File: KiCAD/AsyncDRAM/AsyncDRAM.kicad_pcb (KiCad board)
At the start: 2 copper layers, 54.6 x 33.7 mm, 14 parts, among them J1 UART, J2 SPI, J3 UPDI, J4 POWER

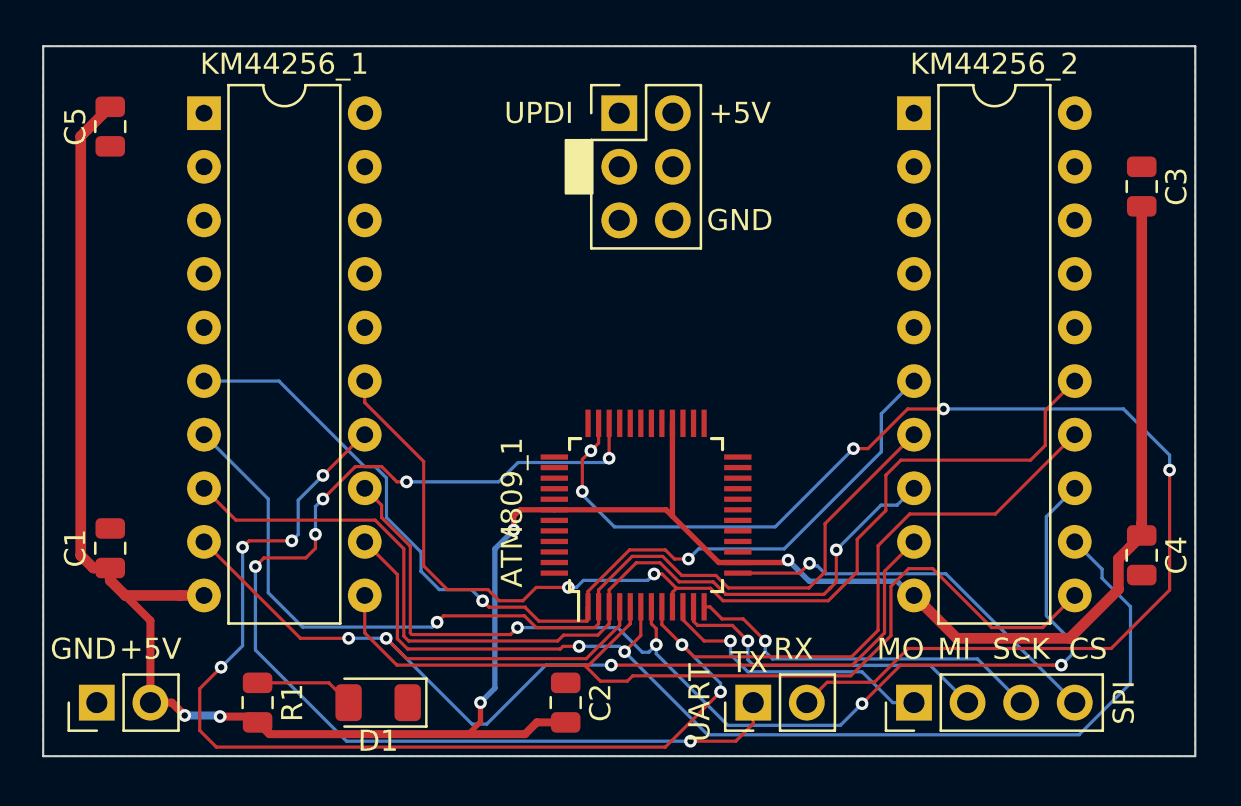
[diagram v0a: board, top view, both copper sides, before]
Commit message: PCB Routing Update
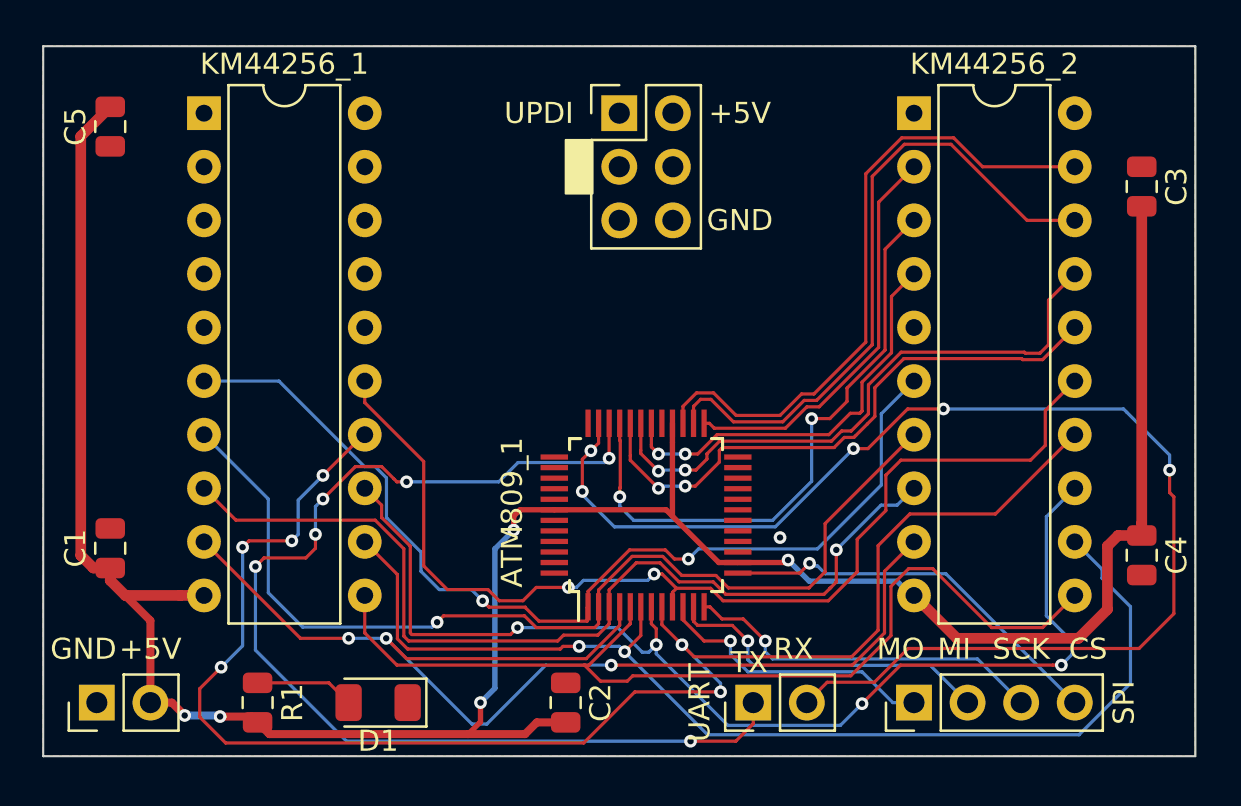
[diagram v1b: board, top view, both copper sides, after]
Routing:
- net D6: track 0.00 -> 31.1 mm
- net D7: track 0.00 -> 30.8 mm
- net ~W: track 0.00 -> 29.3 mm, vias 0 -> 2
- net ~CAS: track 0.00 -> 28.4 mm, vias 0 -> 2
- net ~OE: track 0.00 -> 27.8 mm, vias 0 -> 2
- net ~RAS: track 0.00 -> 19.6 mm, vias 0 -> 2
- net D5: track 0.00 -> 19.2 mm
- net RxD: track 61.2 -> 62.1 mm
- net A0: track 46.9 -> 47.9 mm
- net +5V: track 121.6 -> 122.5 mm
- net A7: track 75.3 -> 74.8 mm
- net GND: vias 0 -> 1

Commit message: Update PCB Routing
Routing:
- net D0: track 0.00 -> 41.2 mm, vias 0 -> 1
- net D1: track 0.00 -> 40.3 mm, vias 0 -> 2
- net D3: track 0.00 -> 36.5 mm, vias 0 -> 1
- net D2: track 0.00 -> 30.9 mm, vias 0 -> 1
- net D4: track 0.00 -> 28.2 mm, vias 0 -> 1
- net ~W: track 29.3 -> 31.8 mm
- net RxD: track 62.1 -> 64.4 mm
- net +5V: track 122.5 -> 124.1 mm, vias 5 -> 6
- net A8: track 50.6 -> 50.0 mm
- net GND: vias 1 -> 0
